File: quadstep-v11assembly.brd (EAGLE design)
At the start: 50 x 50 mm, 106 parts, among them U1 A4983, U2 A4983, U3 A4983, U4 A4983, X1 MSTBA4, X2 MSTBA4, X3 MSTBA4, X4 MSTBA4

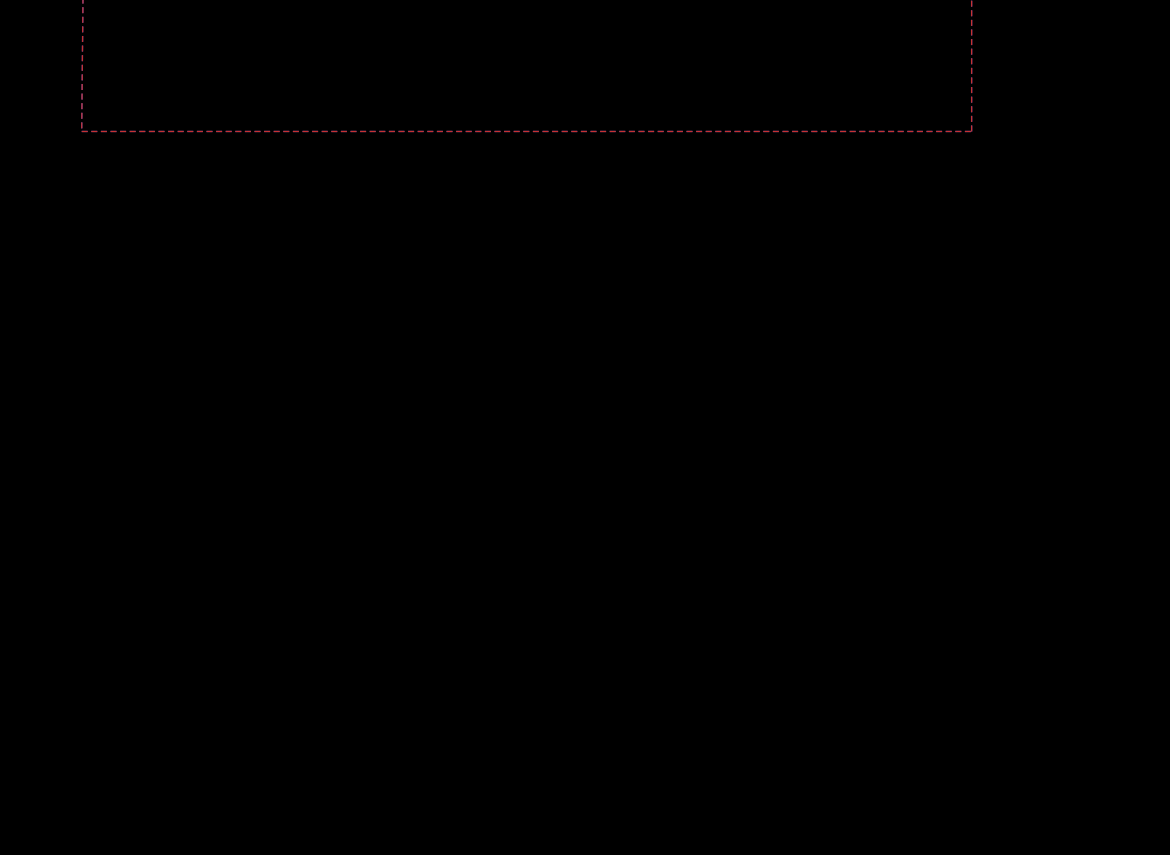
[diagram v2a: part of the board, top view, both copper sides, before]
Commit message: Adding a uC with USB
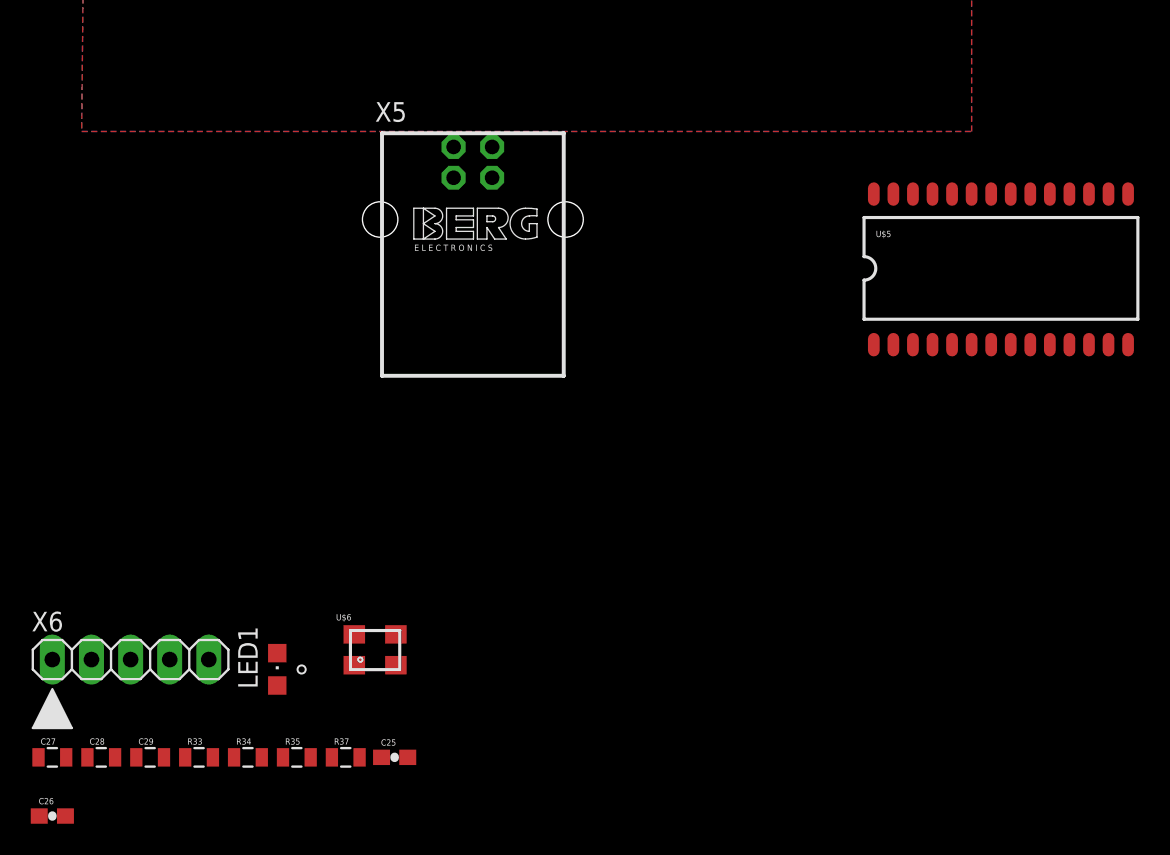
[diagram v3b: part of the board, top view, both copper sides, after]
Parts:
- added C25, C26: 8pF, SparkFun:0603-CAP
- added C27, C28, C29: 100nF, SparkFun:0805
- added LED1: (no value), led:CHIPLED_0805
- added R33, R34, R35, R37: 10k, SparkFun:0805
- added U$5: PIC18F2455SMD, SparkFun:SO-28W
- added U$6: CRYSTAL-SMD- 12MHz, crystal:CRYSTAL-SMD-3.2X2.5
- added X5: (no value), con-berg:PN61729
- added X6: ICSP-5, ICSP:M05
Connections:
- new net !MCLR: R34.2, U$5.1, X6.1
- new net D+: U$5.16, X5.3
- new net D-: U$5.15, X5.2
- new net DOUT1: U$5.17
- new net DOUT2: U$5.25
- new net IN1: U$5.2
- new net IN2: U$5.3
- new net IN3: U$5.4
- new net IN4: U$5.5
- new net LED: R33.2, U$5.21
- new net N$54: LED1.A, R33.1
- new net OSC1: C26.1, U$5.9, U$6.3
- new net OSC2: C25.1, U$5.10, U$6.1
- new net PGC: U$5.27, X6.5
- new net PGD: U$5.28, X6.4
- new net RL1: U$5.7
- new net RL2: U$5.6
- new net RL3: U$5.13
- new net RL4: U$5.12
- new net SCLK1: U$5.18
- new net SCLK2: U$5.26
- new net USB_SENSE: R35.2, U$5.22
- new net VBUS: R35.1, R37.1, X5.1
- new net VDD: R34.1, U$5.20, X6.2
- new net VUSB: C27.2, C28.2, C29.2, U$5.14
- net GND: now also C25.2, C26.2, C27.1, C28.1, C29.1, LED1.C, R37.2, U$5.19, U$5.8, U$6.2, U$6.4, X5.4, X6.3
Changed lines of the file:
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@@
 <element name="R31" library="SparkFun" package="R2010" value=".11" x="42.2275" y="-13.97" rot="R90"/>
 <element name="R32" library="SparkFun" package="0603-RES" value="10k" x="28.575" y="-13.97"/>
+<element name="U$6" library="crystal" package="CRYSTAL-SMD-3.2X2.5" value="CRYSTAL-SMD- 12MHz" x="15.875" y="-93.98"/>
+<element name="C25" library="SparkFun" package="0603-CAP" value="8pF" x="17.145" y="-100.965"/>
+<element name="C26" library="SparkFun" package="0603-CAP" value="8pF" x="-5.08" y="-104.775"/>
+<element name="X6" library="ICSP" package="M05" value="ICSP-5" x="-5.08" y="-94.615"/>
+<element name="R33" library="SparkFun" package="0805" value="10k" x="4.445" y="-100.965"/>
+<element name="LED1" library="led" package="CHIPLED_0805" value="" x="9.525" y="-95.25"/>
+<element name="U$5" library="SparkFun" package="SO-28W" value="PIC18F2455SMD" x="56.515" y="-69.215"/>
+<element name="X5" library="con-berg" package="PN61729" value="" x="22.225" y="-66.04">
+<attribute name="OC_NEWARK" value="unknown" x="-3.81" y="-80.01" size="1.778" layer="27" display="off"/>
+<attribute name="MPN" value="" x="-3.81" y="-80.01" size="1.778" layer="27" display="off"/>
+<attribute name="MF" value="" x="-3.81" y="-80.01" size="1.778" layer="27" display="off"/>
+<attribute name="OC_FARNELL" value="unknown" x="-3.81" y="-80.01" size="1.778" layer="27" display="off"/>
+</element>
+<element name="R34" library="SparkFun" package="0805" value="10k" x="7.62" y="-100.965"/>
+<element name="C27" library="SparkFun" package="0805" value="100nF" x="-5.08" y="-100.965"/>
+<element name="R35" library="SparkFun" package="0805" value="10k" x="10.795" y="-100.965"/>
+<element name="R37" library="SparkFun" package="0805" value="10k" x="13.97" y="-100.965"/>
+<element name="C28" library="SparkFun" package="0805" value="100nF" x="-1.905" y="-100.965"/>
+<element name="C29" library="SparkFun" package="0805" value="100nF" x="1.27" y="-100.965"/>
 </elements>
 <signals>
@@
 <via x="36.5125" y="-13.97" extent="1-16" drill="0.508"/>
 <via x="36.5125" y="-15.24" extent="1-16" drill="0.508"/>
-<wire x1="39.37" y1="34.66" x2="34.1376" y2="43.2816" width="0" layer="19" extent="1-1"/>
+<contactref element="U$6" pad="2"/>
+<contactref element="U$5" pad="8"/>
+<contactref element="U$5" pad="19"/>
+<contactref element="U$6" pad="2"/>
+<contactref element="U$6" pad="4"/>
+<contactref element="C26" pad="2"/>
+<contactref element="C25" pad="2"/>
+<contactref element="X5" pad="4"/>
+<contactref element="X6" pad="3"/>
+<contactref element="LED1" pad="C"/>
+<contactref element="C27" pad="1"/>
+<contactref element="C29" pad="1"/>
+<contactref element="C28" pad="1"/>
+<contactref element="R37" pad="2"/>
+<wire x1="-2.805" y1="-100.965" x2="-4.23" y2="-104.775" width="0" layer="19" extent="1-1"/>
+<wire x1="-5.98" y1="-100.965" x2="-2.805" y2="-100.965" width="0" layer="19" extent="1-1"/>
+<wire x1="0.37" y1="-100.965" x2="-2.805" y2="-100.965" width="0" layer="19" extent="1-1"/>
+<wire x1="0" y1="-94.615" x2="0.37" y2="-100.965" width="0" layer="19" extent="1-1"/>
+<wire x1="57.15" y1="-74.168" x2="0" y2="-94.615" width="0" layer="19" extent="1-1"/>
+<wire x1="9.525" y1="-94.2" x2="57.15" y2="-74.168" width="0" layer="19" extent="1-1"/>
+<wire x1="14.525" y1="-92.98" x2="9.525" y2="-94.2" width="0" layer="19" extent="1-1"/>
+<wire x1="17.225" y1="-94.98" x2="14.525" y2="-92.98" width="0" layer="19" extent="1-1"/>
+<wire x1="17.995" y1="-100.965" x2="17.225" y2="-94.98" width="0" layer="19" extent="1-1"/>
+<wire x1="14.87" y1="-100.965" x2="17.995" y2="-100.965" width="0" layer="19" extent="1-1"/>
+<wire x1="59.69" y1="-64.389" x2="57.15" y2="-74.168" width="0" layer="19" extent="1-1"/>
+<wire x1="23.475" y1="-63.33" x2="59.69" y2="-64.389" width="0" layer="19" extent="1-1"/>
+<wire x1="7.3025" y1="-46.015" x2="23.475" y2="-63.33" width="0" layer="19" extent="1-1"/>
+<wire x1="27.7368" y1="18.15" x2="21.77" y2="-1.69" width="0" layer="19" extent="1-1"/>
+<wire x1="23.1902" y1="22.8926" x2="27.7368" y2="18.15" width="0" layer="19" extent="1-1"/>
+<wire x1="21.3868" y1="19.8264" x2="23.1902" y2="22.8926" width="0" layer="19" extent="1-1"/>
+<wire x1="40.7924" y1="26.0676" x2="27.7368" y2="18.15" width="0" layer="19" extent="1-1"/>
+<wire x1="39.37" y1="34.66" x2="40.7924" y2="26.0676" width="0" layer="19" extent="1-1"/>
 <wire x1="40.64" y1="34.91" x2="39.37" y2="34.66" width="0" layer="19" extent="1-1"/>
-<wire x1="40.7924" y1="26.0676" x2="39.37" y2="34.66" width="0" layer="19" extent="1-1"/>
+<wire x1="34.1376" y1="43.2816" x2="39.37" y2="34.66" width="0" layer="19" extent="1-1"/>
 <wire x1="20.32" y1="43.4676" x2="34.1376" y2="43.2816" width="0" layer="19" extent="1-1"/>
 <wire x1="6.096" y1="37.973" x2="20.32" y2="43.4676" width="0" layer="19" extent="1-1"/>
-<wire x1="27.7368" y1="18.15" x2="40.7924" y2="26.0676" width="0" layer="19" extent="1-1"/>
-<wire x1="23.1902" y1="22.8926" x2="27.7368" y2="18.15" width="0" layer="19" extent="1-1"/>
-<wire x1="21.3868" y1="19.8264" x2="23.1902" y2="22.8926" width="0" layer="19" extent="1-1"/>
 <wire x1="6.35" y1="53.99" x2="6.096" y2="37.973" width="0" layer="19" extent="1-1"/>
-<wire x1="21.77" y1="-1.69" x2="27.7368" y2="18.15" width="0" layer="19" extent="1-1"/>
 </signal>
 <signal name="N$1">
@@
 <wire x1="27.725" y1="-15.625" x2="27.76" y2="-15.66" width="0.254" layer="1"/>
 </signal>
+<signal name="VDD">
+<contactref element="U$5" pad="20"/>
+<contactref element="U$5" pad="20"/>
+<contactref element="X6" pad="2"/>
+<contactref element="R34" pad="1"/>
+<wire x1="6.72" y1="-100.965" x2="-2.54" y2="-94.615" width="0" layer="19" extent="1-1"/>
+<wire x1="58.42" y1="-64.389" x2="-2.54" y2="-94.615" width="0" layer="19" extent="1-1"/>
+</signal>
+<signal name="D+">
+<contactref element="U$5" pad="16"/>
+<contactref element="X5" pad="3"/>
+<wire x1="20.975" y1="-63.33" x2="63.5" y2="-64.389" width="0" layer="19" extent="1-1"/>
+</signal>
+<signal name="D-">
+<contactref element="U$5" pad="15"/>
+<contactref element="X5" pad="2"/>
+<wire x1="20.975" y1="-61.33" x2="64.77" y2="-64.389" width="0" layer="19" extent="1-1"/>
+</signal>
+<signal name="VUSB">
+<contactref element="U$5" pad="14"/>
+<contactref element="C27" pad="2"/>
+<contactref element="C29" pad="2"/>
+<contactref element="C28" pad="2"/>
+<wire x1="-1.005" y1="-100.965" x2="-4.18" y2="-100.965" width="0" layer="19" extent="1-1"/>
+<wire x1="2.17" y1="-100.965" x2="-1.005" y2="-100.965" width="0" layer="19" extent="1-1"/>
+<wire x1="64.77" y1="-74.168" x2="2.17" y2="-100.965" width="0" layer="19" extent="1-1"/>
+</signal>
+<signal name="OSC2">
+<contactref element="U$5" pad="10"/>
+<contactref element="U$6" pad="1"/>
+<contactref element="C25" pad="1"/>
+<wire x1="14.525" y1="-94.98" x2="59.69" y2="-74.168" width="0" layer="19" extent="1-1"/>
+<wire x1="16.295" y1="-100.965" x2="14.525" y2="-94.98" width="0" layer="19" extent="1-1"/>
+</signal>
+<signal name="OSC1">
+<contactref element="U$5" pad="9"/>
+<contactref element="U$6" pad="3"/>
+<contactref element="C26" pad="1"/>
+<wire x1="58.42" y1="-74.168" x2="-5.93" y2="-104.775" width="0" layer="19" extent="1-1"/>
+<wire x1="17.225" y1="-92.98" x2="58.42" y2="-74.168" width="0" layer="19" extent="1-1"/>
+</signal>
+<signal name="!MCLR">
+<contactref element="U$5" pad="1"/>
+<contactref element="X6" pad="1"/>
+<contactref element="R34" pad="2"/>
+<wire x1="48.26" y1="-74.168" x2="-5.08" y2="-94.615" width="0" layer="19" extent="1-1"/>
+<wire x1="8.52" y1="-100.965" x2="-5.08" y2="-94.615" width="0" layer="19" extent="1-1"/>
+</signal>
+<signal name="DOUT2">
+<contactref element="U$5" pad="25"/>
+</signal>
+<signal name="SCLK1">
+<contactref element="U$5" pad="18"/>
+</signal>
+<signal name="DOUT1">
+<contactref element="U$5" pad="17"/>
+</signal>
+<signal name="N$54">
+<contactref element="LED1" pad="A"/>
+<contactref element="R33" pad="1"/>
+<wire x1="9.525" y1="-96.3" x2="3.545" y2="-100.965" width="0" layer="19" extent="1-1"/>
+</signal>
+<signal name="LED">
+<contactref element="R33" pad="2"/>
+<contactref element="U$5" pad="21"/>
+<wire x1="57.15" y1="-64.389" x2="5.345" y2="-100.965" width="0" layer="19" extent="1-1"/>
+</signal>
+<signal name="SCLK2">
+<contactref element="U$5" pad="26"/>
+</signal>
+<signal name="RL1">
+<contactref element="U$5" pad="7"/>
+</signal>
+<signal name="RL2">
+<contactref element="U$5" pad="6"/>
+</signal>
+<signal name="RL3">
+<contactref element="U$5" pad="13"/>
+</signal>
+<signal name="RL4">
+<contactref element="U$5" pad="12"/>
+</signal>
+<signal name="IN1">
+<contactref element="U$5" pad="2"/>
+</signal>
+<signal name="IN2">
+<contactref element="U$5" pad="3"/>
+</signal>
+<signal name="IN3">
+<contactref element="U$5" pad="4"/>
+</signal>
+<signal name="IN4">
+<contactref element="U$5" pad="5"/>
+</signal>
+<signal name="PGD">
+<contactref element="U$5" pad="28"/>
+<contactref element="X6" pad="4"/>
+<wire x1="48.26" y1="-64.389" x2="2.54" y2="-94.615" width="0" layer="19" extent="1-1"/>
+</signal>
+<signal name="PGC">
+<contactref element="U$5" pad="27"/>
+<contactref element="X6" pad="5"/>
+<wire x1="49.53" y1="-64.389" x2="5.08" y2="-94.615" width="0" layer="19" extent="1-1"/>
+</signal>
+<signal name="VBUS">
+<contactref element="R35" pad="1"/>
+<contactref element="R37" pad="1"/>
+<contactref element="X5" pad="1"/>
+<wire x1="13.07" y1="-100.965" x2="9.895" y2="-100.965" width="0" layer="19" extent="1-1"/>
+<wire x1="23.475" y1="-61.33" x2="9.895" y2="-100.965" width="0" layer="19" extent="1-1"/>
+</signal>
+<signal name="USB_SENSE">
+<contactref element="R35" pad="2"/>
+<contactref element="U$5" pad="22"/>
+<wire x1="55.88" y1="-64.389" x2="11.695" y2="-100.965" width="0" layer="19" extent="1-1"/>
+</signal>
 </signals>

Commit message: Improving the layout
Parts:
- removed U$5: PIC18F2455SMD, SparkFun:SO-28W
- added IC2: PIC18F2455_28W, microchip:SO28W
- C11, C16, C17, C18, C23, C24, C5, C6: device SparkFun:0402-CAP -> SparkFun:0603-CAP
- R61, R62: device SparkFun:0402-RES -> SparkFun:0603-RES
- moved C26 236.7 mm to (17.8, 130.8), flipped to the bottom, turned to 270 degrees
- moved C27 232.6 mm to (14.0, 130.8), flipped to the bottom, turned to 270 degrees
- moved C28 229.2 mm to (14.0, 127.6), flipped to the bottom, turned to 270 degrees
- moved C29 225.8 mm to (14.0, 124.5), flipped to the bottom, turned to 270 degrees
- moved R33 222.5 mm to (14.0, 121.3), flipped to the bottom, turned to 270 degrees
- moved R34 219.2 mm to (14.0, 118.1), flipped to the bottom, turned to 270 degrees
- moved R35 215.9 mm to (14.0, 114.9), flipped to the bottom, turned to 270 degrees
- moved LED1 215.8 mm to (24.1, 120.0), flipped to the bottom, turned to 270 degrees
- moved U$6 215.5 mm to (34.9, 120.7), flipped to the bottom, turned to 270 degrees
- moved R37 212.7 mm to (14.0, 111.8), flipped to the bottom, turned to 270 degrees
- moved C25 209.6 mm to (14.0, 108.6), flipped to the bottom, turned to 270 degrees
- moved X6 183.8 mm to (19.1, 87.6), turned to 90 degrees
- moved X5 178.9 mm to (58.1, 109.2), turned to 180 degrees
- moved JP9 102.0 mm to (97.2, 47.0), turned to 90 degrees
- moved JP11 98.8 mm to (-69.8, 2.54), turned to 90 degrees
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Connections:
- removed net IN1: U$5.2
- removed net IN2: U$5.3
- net !MCLR: now also IC2.1; no longer U$5.1
- net D+: now also IC2.16; no longer U$5.16
- net D-: now also IC2.15; no longer U$5.15
- net DIR-1: now also IC2.2
- net DIR-2: now also U1.P$19; no longer U2.P$19
- net DIR-3: now also U2.P$19; no longer U1.P$19
- net DOUT1: now also IC2.17; no longer U$5.17
- net DOUT2: now also IC2.25; no longer U$5.25
- net GND: now also IC2.19, IC2.8; no longer U$5.19, U$5.8
- net IN3: now also IC2.4; no longer U$5.4
- net IN4: now also IC2.5; no longer U$5.5
- net LED: now also IC2.21; no longer U$5.21
- net MS1-2: now also R5.2, SJ4.2, U1.P$9; no longer R19.2, SJ8.2, U2.P$9
- net MS1-3: now also R19.2, SJ8.2, U2.P$9; no longer R5.2, SJ4.2, U1.P$9
- net MS2-2: now also R4.2, SJ3.2, U1.P$10; no longer R18.2, SJ7.2, U2.P$10
- net MS2-3: now also R18.2, SJ7.2, U2.P$10; no longer R4.2, SJ3.2, U1.P$10
- net MS3-2: now also R3.2, SJ2.2, U1.P$11; no longer R17.2, SJ6.2, U2.P$11
- net MS3-3: now also R17.2, SJ6.2, U2.P$11; no longer R3.2, SJ2.2, U1.P$11
- net N$10: now also X2.3; no longer X3.3
- net N$11: now also X2.2; no longer X3.2
- net N$12: now also X2.1; no longer X3.1
- net N$13: now also X2.4; no longer X3.4
- net N$34: now also X3.3; no longer X2.3
- net N$35: now also X3.2; no longer X2.2
- net N$36: now also X3.1; no longer X2.1
- net N$37: now also X3.4; no longer X2.4
- net OSC1: now also IC2.9; no longer U$5.9
- net OSC2: now also IC2.10; no longer U$5.10
- net PGC: now also IC2.27; no longer U$5.27
- net PGD: now also IC2.28; no longer U$5.28
- net RL1: now also IC2.7; no longer U$5.7
- net RL2: now also IC2.6; no longer U$5.6
- net RL3: now also IC2.13; no longer U$5.13
- net RL4: now also IC2.12; no longer U$5.12
- net RST-2: now also R6.2, SJ5.2, U1.P$12; no longer R20.2, SJ9.2, U2.P$12
- net RST-3: now also R20.2, SJ9.2, U2.P$12; no longer R6.2, SJ5.2, U1.P$12
- net SCLK1: now also IC2.18; no longer U$5.18
- net SCLK2: now also IC2.26; no longer U$5.26
- net STP-1: now also IC2.3
- net STP-2: now also U1.P$16; no longer U2.P$16
- net STP-3: now also U2.P$16; no longer U1.P$16
- net USB_SENSE: now also IC2.22; no longer U$5.22
- net VDD: now also IC2.20; no longer U$5.20
- net VUSB: now also IC2.14; no longer U$5.14
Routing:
- net VCC: track 87.3 -> 246.3 mm
- net SLP: track 0.00 -> 130.1 mm, vias 0 -> 4
- net VOUT: track 82.8 -> 196.6 mm
- net EN: track 7.36 -> 112.4 mm
- net DIR-1: track 0.00 -> 17.7 mm
- net DIR-4: track 0.00 -> 17.7 mm
- net DIR-3: track 0.00 -> 17.7 mm
- net DIR-2: track 0.00 -> 17.7 mm
- net GND: track 105.6 -> 120.8 mm, vias 60 -> 92
- net STP-2: track 2.61 -> 15.8 mm, vias 1 -> 0
- net STP-1: track 2.61 -> 15.8 mm, vias 1 -> 0
- net STP-3: track 2.61 -> 15.8 mm, vias 1 -> 0
- net STP-4: track 2.61 -> 15.8 mm, vias 1 -> 0
- net N$22: track 7.79 -> 13.5 mm, vias 0 -> 2
- net N$7: track 7.79 -> 13.5 mm, vias 0 -> 2
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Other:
- board size 50 x 50 mm -> 100 x 50 mm

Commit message: Layout ....
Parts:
- removed JP22: (no value), SparkFun:1X08
- added JP1: (no value), pinhead:1X10
- added JP2, JP3: (no value), pinhead:2X06
- added X10, X7, X8, X9: 22-23-2041, con-molex:22-23-2041
- added X11: MSTBA4, con-phoenix-508:MSTBA4
- moved R36 108.1 mm to (51.4, 33.0), turned to 90 degrees
- moved LED5 106.0 mm to (48.9, 33.0)
- moved C31 104.5 mm to (62.7, 43.2), turned to 180 degrees
- moved C28 96.9 mm to (22.9, 31.1), flipped to the top, turned to 0 degrees
- moved C27 96.3 mm to (22.9, 34.9), flipped to the top, turned to 0 degrees
- moved IC1 93.6 mm to (52.6, 43.6), turned to 0 degrees
- moved C29 91.9 mm to (22.9, 33.0), flipped to the top, turned to 0 degrees
- moved X5 83.0 mm to (12.4, 40.0)
- moved U$6 68.2 mm to (28.6, 52.7), turned to 180 degrees
- moved C32 66.5 mm to (52.1, 37.5), turned to 270 degrees
- moved C30 64.1 mm to (50.2, 37.5), turned to 270 degrees
- moved R33 63.5 mm to (22.9, 58.4), turned to 180 degrees
- moved R34 60.9 mm to (26.0, 58.4), turned to 180 degrees
- moved R35 58.5 mm to (29.2, 58.4), turned to 180 degrees
- moved R37 56.4 mm to (32.4, 58.4), turned to 180 degrees
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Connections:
- removed net DOUT1: IC2.17
- removed net DOUT2: IC2.25
- removed net IN3: IC2.4
- removed net IN4: IC2.5
- removed net RL1: IC2.7
- removed net RL2: IC2.6
- removed net RL3: IC2.13
- removed net RL4: IC2.12
- removed net SCLK1: IC2.18
- removed net SCLK2: IC2.26
- new net N$55: JP1.1
- new net N$56: JP1.2
- new net N$57: JP1.3
- new net N$58: JP1.4
- new net N$59: JP1.5
- new net N$60: JP1.6
- new net N$61: JP1.7
- new net N$62: JP1.8
- new net N$63: JP1.9
- new net N$64: JP1.10
- net DIR-1: no longer IC2.2
- net LED: no longer IC2.21
- net STP-1: no longer IC2.3
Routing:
- removed copper zone on layer 1, net VOUT
- removed copper zone on layer 16, net VOUT
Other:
- board text removed: "GND"
- board text removed: "VIN"
